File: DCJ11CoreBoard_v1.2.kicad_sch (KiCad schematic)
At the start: 200 parts, among them Q1 BSS138W, Q2 BSS84, Q3 BSS138W, U1 DCJ11, U10 SY8089AAAC, U11 SN74CB3T3245PWR, U12 SN74CB3T3245PWR, U13 SN74CB3T3245PWR, U14 ME6211A12M3G-N, U15 ME6211A25M3G-N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

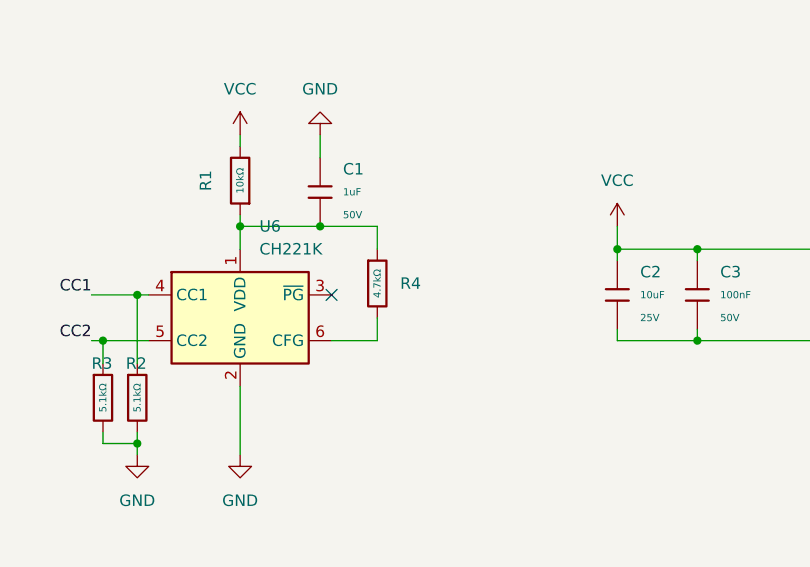
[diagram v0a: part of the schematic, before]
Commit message: modify the value of PD negotiation chip's cfg resistor
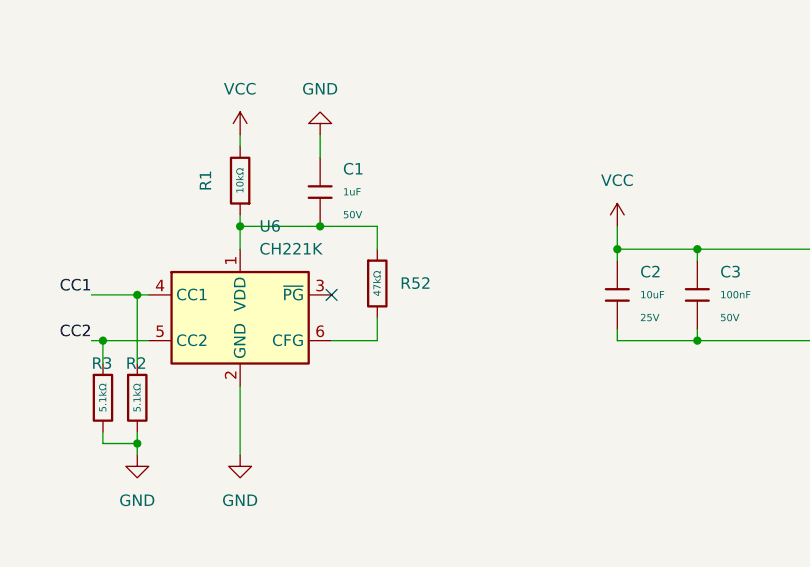
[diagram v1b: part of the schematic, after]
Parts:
- removed R4: 4.7kΩ, PCM_JLCPCB:R_0603, symbol PCM_JLCPCB-Resistors:0603,4.7kΩ
- added R52: 47kΩ, PCM_JLCPCB:R_0402, symbol PCM_JLCPCB-Resistors:0402,47kΩ
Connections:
- net at C1.2, R1.1, U6.1 (VDD): now also R52.1
- net at U6.6 (CFG): now also R52.2
